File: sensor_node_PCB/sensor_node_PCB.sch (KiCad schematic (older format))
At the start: 23 parts

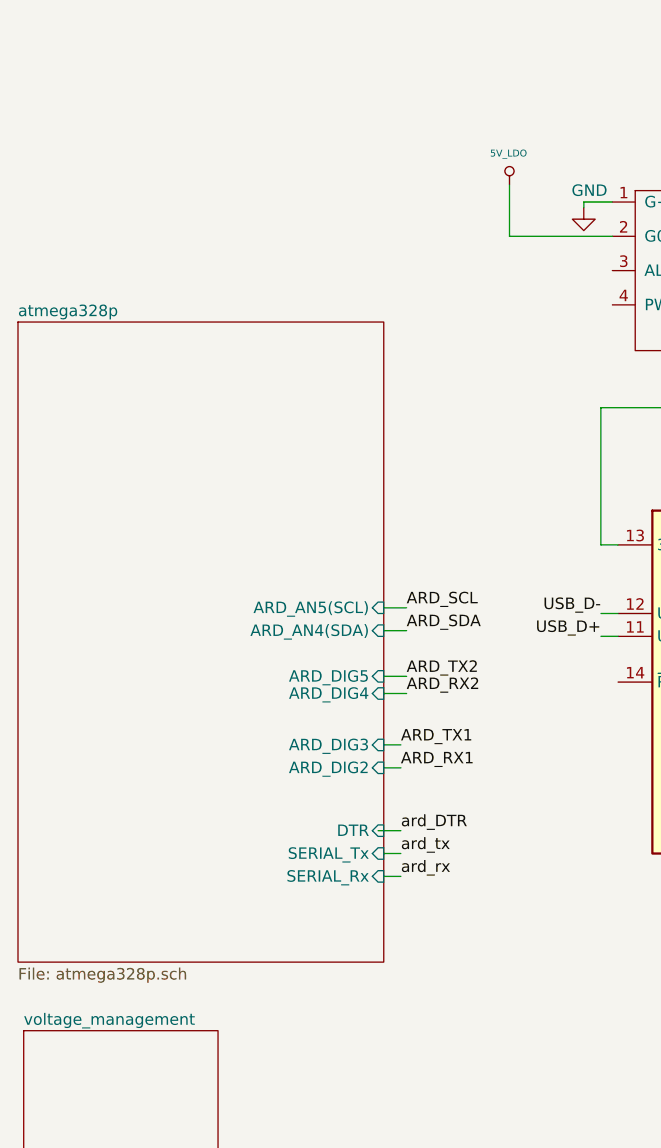
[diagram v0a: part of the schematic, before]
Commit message: ADDED BREAKOUT PINS
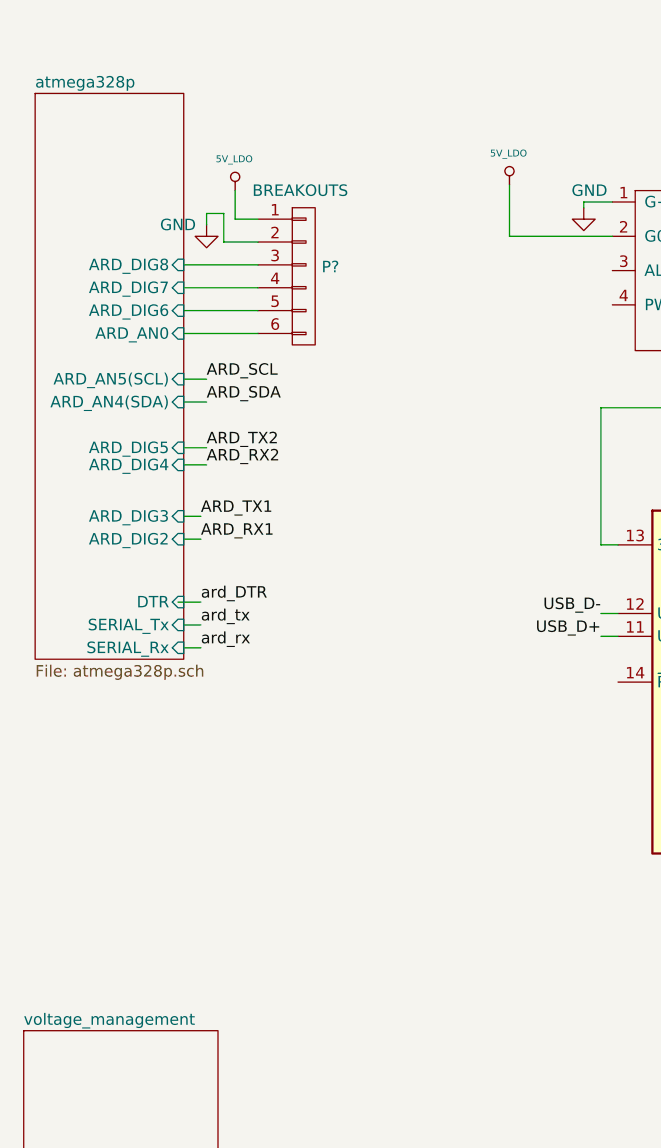
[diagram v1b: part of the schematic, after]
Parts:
- added P?: BREAKOUTS, symbol Arduino_Uno_R3_From_Scratch-rescue:CONN_01X06
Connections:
- net 5V_LDO: now also P?.1 (P1)
- net GND: now also P?.2 (P2)
- new net atmega328p/ARD_AN0: P?.6 (P6)
- new net atmega328p/ARD_DIG6: P?.5 (P5)
- new net atmega328p/ARD_DIG7: P?.4 (P4)
- new net atmega328p/ARD_DIG8: P?.3 (P3)
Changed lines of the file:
@@
 $EndComp
-$Sheet
-S 625  1825 1600 2800
-U 5F4E1E8A
-F0 "atmega328p" 50
-F1 "atmega328p.sch" 50
-F2 "SERIAL_Rx" I R 2225 4250 50
-F3 "SERIAL_Tx" I R 2225 4150 50
-F4 "DTR" I R 2225 4050 50
-F5 "ARD_DIG2" I R 2225 3775 50
-F6 "ARD_DIG3" I R 2225 3675 50
-F7 "ARD_DIG4" I R 2225 3450 50
-F8 "ARD_DIG5" I R 2225 3375 50
-F9 "ARD_AN4(SDA)" I R 2225 3175 50
-F10 "ARD_AN5(SCL)" I R 2225 3075 50
-$EndSheet
 $Sheet
 S 650  4925 850  850
@@
 	1    0    0    -1
 $EndComp
-Text Label 2300 4150 0    50   ~ 0
+Text Label 1425 3150 0    50   ~ 0
 ard_tx
 Wire Wire Line
-	2225 4150 2300 4150
-Text Label 2300 4250 0    50   ~ 0
+	1350 3150 1425 3150
+Text Label 1425 3250 0    50   ~ 0
 ard_rx
 Wire Wire Line
-	2225 4250 2300 4250
+	1350 3250 1425 3250
 Text Label 4750 2900 0    50   ~ 0
 ard_tx
@@
 Wire Wire Line
 	4650 2900 4750 2900
-Text Label 2300 4050 0    50   ~ 0
+Text Label 1425 3050 0    50   ~ 0
 ard_DTR
 Wire Wire Line
-	2200 4050 2300 4050
+	1325 3050 1425 3050
 Text Label 4750 3200 0    50   ~ 0
 ard_DTR
@@
 Wire Wire Line
 	4175 2500 4050 2500
-Text Label 2300 3675 0    50   ~ 0
+Text Label 1425 2675 0    50   ~ 0
 ARD_TX1
-Text Label 2300 3775 0    50   ~ 0
+Text Label 1425 2775 0    50   ~ 0
 ARD_RX1
 Wire Wire Line
-	2225 3775 2300 3775
-Wire Wire Line
-	2225 3675 2300 3675
+	1350 2775 1425 2775
+Wire Wire Line
+	1350 2675 1425 2675
 $Comp
 L Kicad_symbols:SP485EEN-L_TR U?
@@
 Wire Wire Line
 	3100 1300 3225 1300
-Text Label 2325 3375 0    50   ~ 0
+Text Label 1450 2375 0    50   ~ 0
 ARD_TX2
 Wire Wire Line
-	2225 3375 2325 3375
-Text Label 2325 3450 0    50   ~ 0
+	1350 2375 1450 2375
+Text Label 1450 2450 0    50   ~ 0
 ARD_RX2
 Wire Wire Line
-	2225 3450 2325 3450
+	1350 2450 1450 2450
 Text Label 4450 1600 0    50   ~ 0
 ARD_RX2
@@
 Wire Wire Line
 	9800 2950 9800 3000
-Text Label 2325 3075 0    50   ~ 0
+Text Label 1450 2075 0    50   ~ 0
 ARD_SCL
-Text Label 2325 3175 0    50   ~ 0
+Text Label 1450 2175 0    50   ~ 0
 ARD_SDA
 Wire Wire Line
-	2225 3075 2325 3075
-Wire Wire Line
-	2225 3175 2325 3175
+	1350 2075 1450 2075
+Wire Wire Line
+	1350 2175 1450 2175
 Text Label 10200 2600 0    50   ~ 0
 ARD_SCL
@@
 Wire Wire Line
 	10950 4300 10950 4375
+$Comp
+L Arduino_Uno_R3_From_Scratch-rescue:CONN_01X06 P?
+U 1 1 5F6DB19A
+P 1875 1625
+F 0 "P?" H 1953 1666 50  0000 L CNN
+F 1 "BREAKOUTS" H 1650 2000 50  0000 L CNN
+F 2 "" H 1875 1625 60  0000 C CNN
+F 3 "" H 1875 1625 60  0000 C CNN
+	1    1875 1625
+	1    0    0    -1
+$EndComp
+$Comp
+L Arduino_Uno_R3_From_Scratch-rescue:5V_LDO #PWR?
+U 1 1 5F6DDE3C
+P 1575 1250
+F 0 "#PWR?" H 1575 1340 20  0001 C CNN
+F 1 "5V_LDO" H 1571 1388 30  0000 C CNN
+F 2 "" H 1575 1250 60  0000 C CNN
+F 3 "" H 1575 1250 60  0000 C CNN
+	1    1575 1250
+	1    0    0    -1
+$EndComp
+$Comp
+L Arduino_Uno_R3_From_Scratch-rescue:GND #PWR?
+U 1 1 5F6DF1FF
+P 1450 1400
+F 0 "#PWR?" H 1450 1150 50  0001 C CNN
+F 1 "GND" H 1325 1400 50  0000 C CNN
+F 2 "" H 1450 1400 60  0000 C CNN
+F 3 "" H 1450 1400 60  0000 C CNN
+	1    1450 1400
+	1    0    0    -1
+$EndComp
+Wire Wire Line
+	1575 1250 1575 1375
+Wire Wire Line
+	1575 1375 1675 1375
+Wire Wire Line
+	1675 1475 1525 1475
+Wire Wire Line
+	1525 1475 1525 1350
+Wire Wire Line
+	1525 1350 1450 1350
+Wire Wire Line
+	1450 1350 1450 1400
+Wire Wire Line
+	1350 1575 1675 1575
+Wire Wire Line
+	1350 1675 1675 1675
+Wire Wire Line
+	1350 1775 1675 1775
+Wire Wire Line
+	1350 1875 1675 1875
+$Sheet
+S 700  825  650  2475
+U 5F4E1E8A
+F0 "atmega328p" 50
+F1 "atmega328p.sch" 50
+F2 "SERIAL_Rx" I R 1350 3250 50
+F3 "SERIAL_Tx" I R 1350 3150 50
+F4 "DTR" I R 1350 3050 50
+F5 "ARD_DIG2" I R 1350 2775 50
+F6 "ARD_DIG3" I R 1350 2675 50
+F7 "ARD_DIG4" I R 1350 2450 50
+F8 "ARD_DIG5" I R 1350 2375 50
+F9 "ARD_AN4(SDA)" I R 1350 2175 50
+F10 "ARD_AN5(SCL)" I R 1350 2075 50
+F11 "ARD_DIG6" I R 1350 1775 50
+F12 "ARD_DIG7" I R 1350 1675 50
+F13 "ARD_DIG8" I R 1350 1575 50
+F14 "ARD_AN0" I R 1350 1875 50
+$EndSheet
 $EndSCHEMATC

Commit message: schematic finished
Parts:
- added C?: 1uF, ~, symbol Arduino_Uno_R3_From_Scratch-rescue:C
- added C?: 0.1 uF, ~, symbol Arduino_Uno_R3_From_Scratch-rescue:C
- added C?: 4.7uF, ~, symbol Arduino_Uno_R3_From_Scratch-rescue:C
- added Q?: FDN340P, ~, symbol Arduino_Uno_R3_From_Scratch-rescue:Q_PMOS_GSD
- added R? (x2): 10K, ~, symbol Arduino_Uno_R3_From_Scratch-rescue:R
- added U?: LMV358IDGKR, ~, symbol Arduino_Uno_R3_From_Scratch-rescue:LM358
- added U?: LM1117-3.3, symbol Regulator_Linear:LM1117-3.3
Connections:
- net 3V3_LDO: now also C?.1, U?.2 (-), U?.2 (VO)
- net 5V_LDO: now also C?.1, C?.2, Q?.2 (S), U?.3 (VI), U?.8 (V+)
- net GND: now also C?.1, C?.2, C?.2, R?.1, U?.1 (GND), U?.4 (V-)
- net USBVCC: now also Q?.3 (D)
- net Vin: now also R?.2
- net at U?.13 (3V3OUT), U?.3 (VCCIO): now also U?.14 (~RESET)
- new net: R?.1, R?.2, U?.3 (+)
- new net: Q?.1 (G), U?.1
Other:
- moved on the sheet: C?, D?, F?, J?, Q?, R?, U?

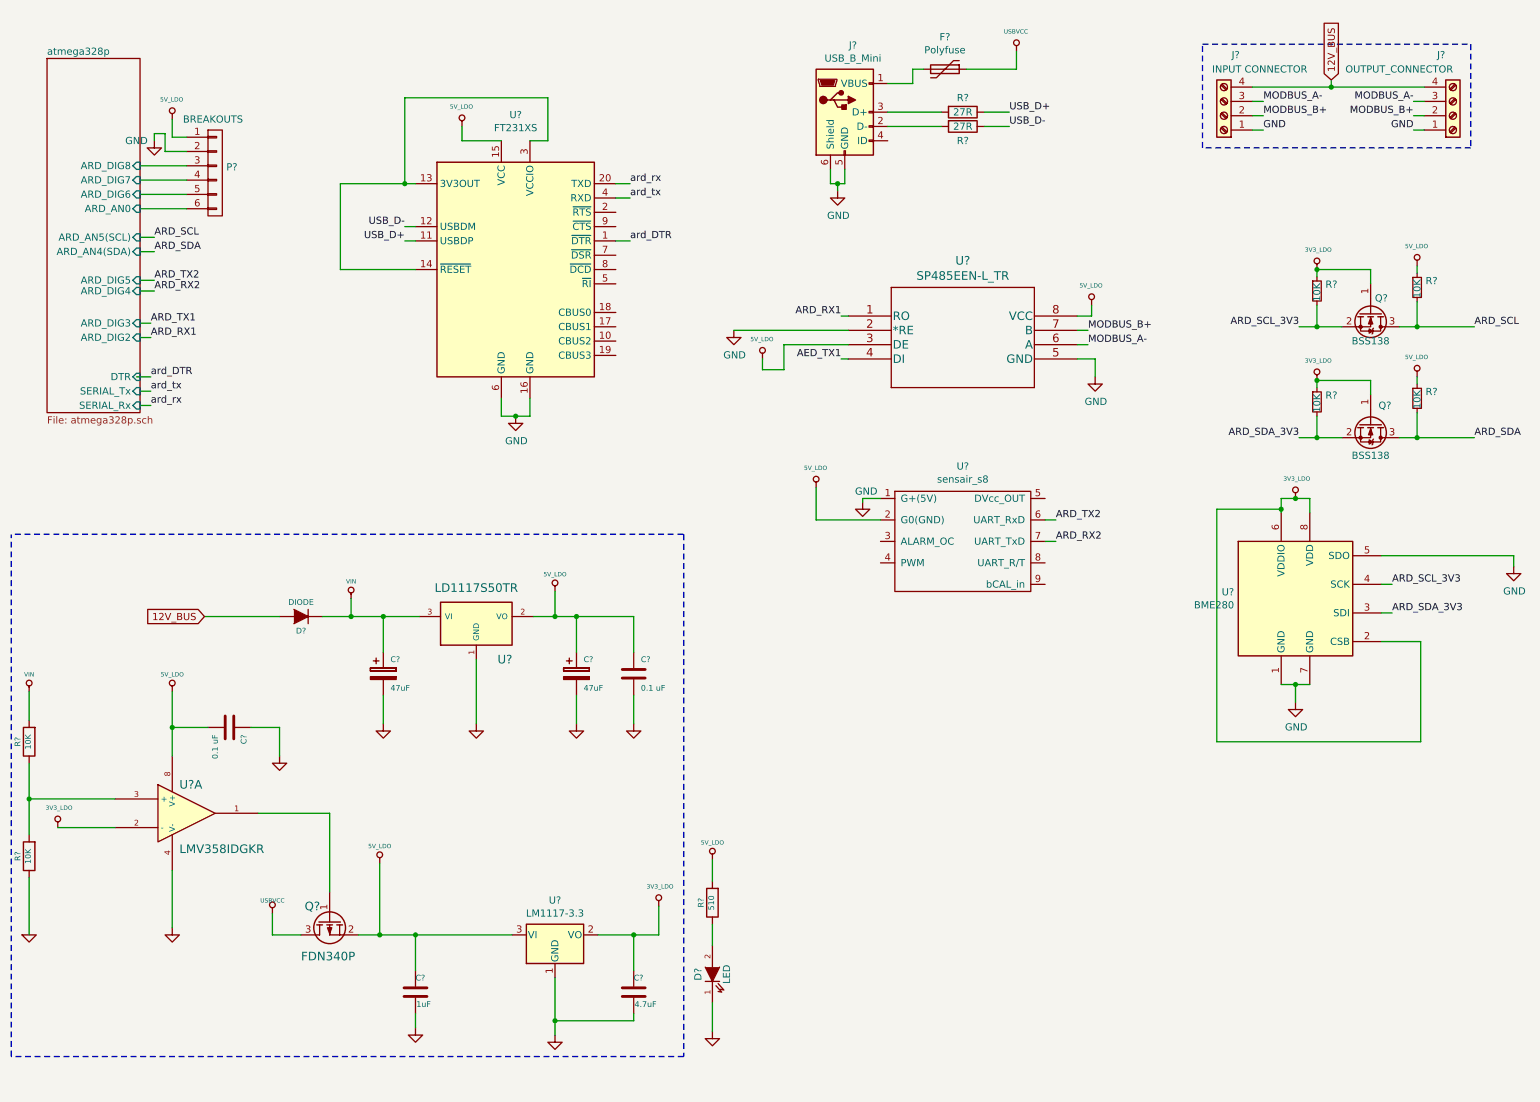
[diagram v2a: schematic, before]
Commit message: assign footprints 80% completed
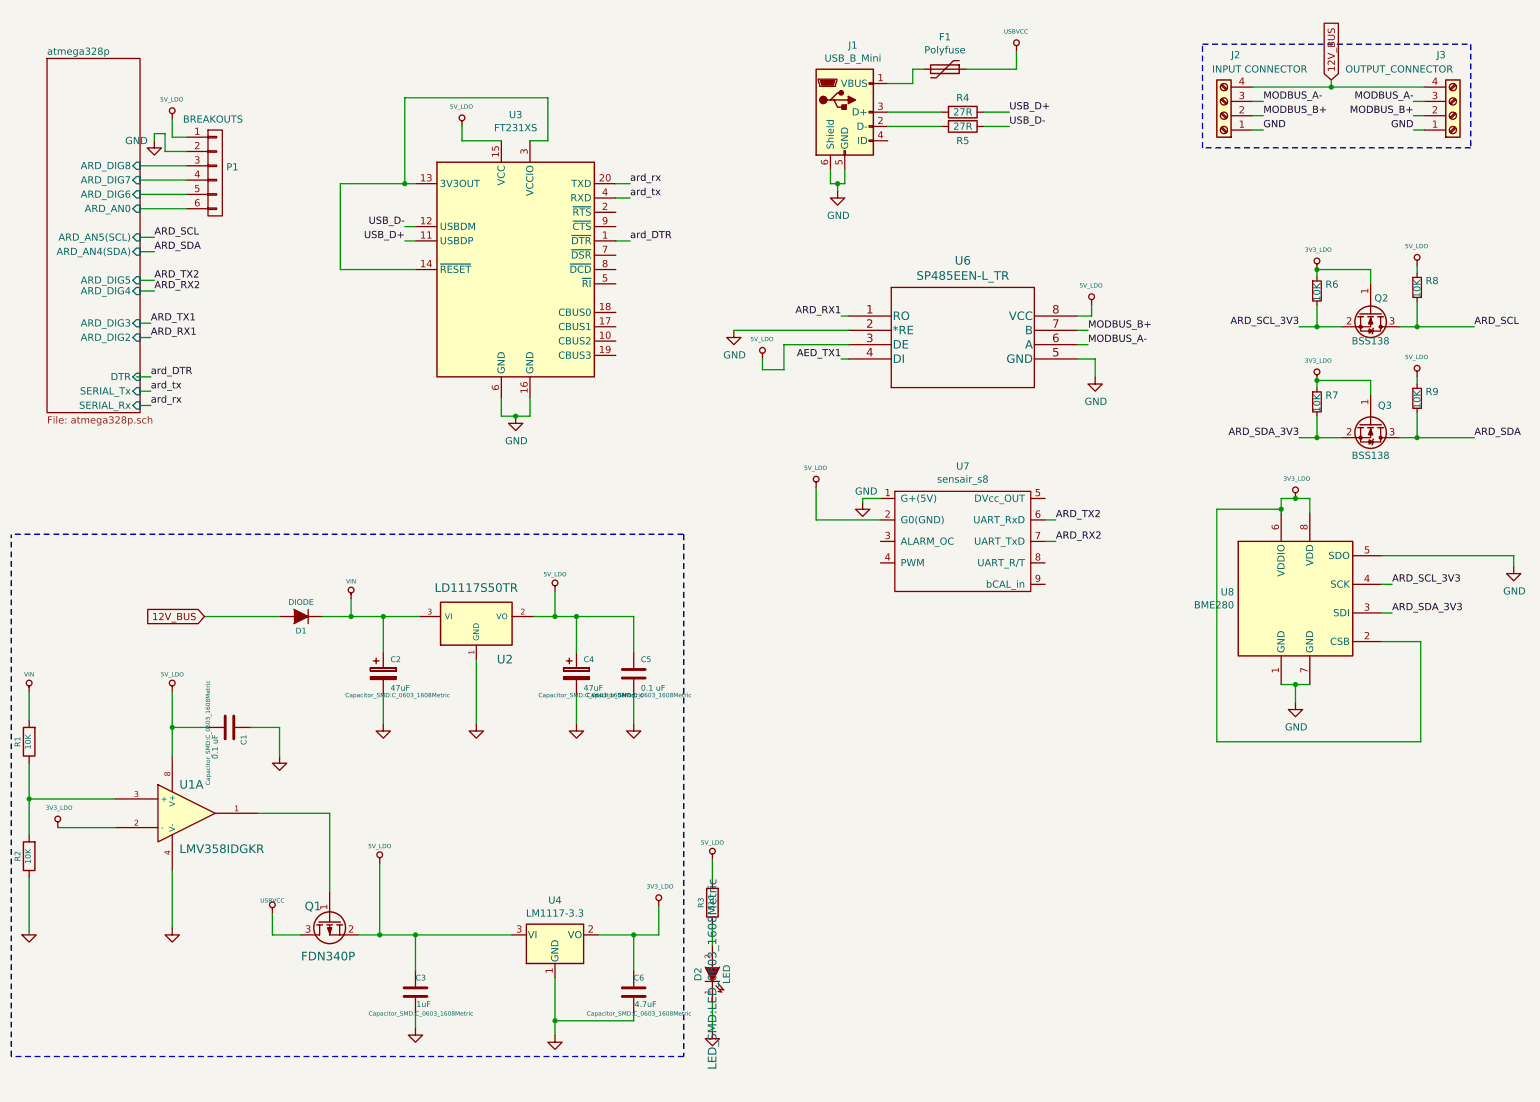
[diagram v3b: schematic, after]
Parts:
- C1, C2, C3, C4, C5, C6: renamed from C?; footprint ~ -> Capacitor_SMD:C_0603_1608Metric
- D1: renamed from D?; footprint ~ -> (none)
- D2: renamed from D?; footprint ~ -> LED_SMD:LED_0603_1608Metric
- F1: renamed from F?; footprint (none) -> Fuse:Fuse_1206_3216Metric
- J1: renamed from J?; footprint (none) -> Connector_USB:USB_Mini-B_Wuerth_65100516121_Horizontal
- P1: renamed from P?; footprint (none) -> Connector_PinHeader_2.54mm:PinHeader_1x06_P2.54mm_Vertical
- Q1: renamed from Q?; footprint ~ -> Package_TO_SOT_SMD:SuperSOT-3
- R1, R2, R3: renamed from R?; footprint ~ -> Resistor_SMD:R_0603_1608Metric
- R4, R5, R6, R7, R8, R9: renamed from R?; footprint (none) -> Resistor_SMD:R_0603_1608Metric
- U1: renamed from U?; footprint ~ -> Package_SO:SOIC-8_3.9x4.9mm_P1.27mm
- U2, U4: renamed from U?; footprint (none) -> Package_TO_SOT_SMD:SOT-223-3_TabPin2
- U6: renamed from U?; footprint NSOIC-8 -> Package_SO:SOIC-8_3.9x4.9mm_P1.27mm
- gave numbers to parts that had none: 7

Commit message: routing started 15%
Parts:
- D1: footprint (none) -> Diode_SMD:D_SOD-123
- J2, J3: footprint (none) -> Connector_Phoenix_MSTB:PhoenixContact_MSTB_2,5_4-GF-5,08_1x04_P5.08mm_Horizontal_ThreadedFlange
- P1: footprint Connector_PinHeader_2.54mm:PinHeader_1x06_P2.54mm_Vertical -> TerminalBlock_Phoenix:TerminalBlock_Phoenix_MPT-0,5-6-2.54_1x06_P2.54mm_Horizontal
- U7: footprint (none) -> kicad_footprints:senseair_s8_v3
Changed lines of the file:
@@
 F 0 "J2" H 8843 800 50  0000 C CNN
 F 1 "INPUT CONNECTOR" H 8675 900 50  0000 C CNN
-F 2 "" H 8925 1225 50  0001 C CNN
+F 2 "Connector_Phoenix_MSTB:PhoenixContact_MSTB_2,5_4-GF-5,08_1x04_P5.08mm_Horizontal_ThreadedFlange" H 8925 1225 50  0001 C CNN
 F 3 "~" H 8925 1225 50  0001 C CNN
 	1    8925 1225
@@
 F 0 "J3" H 10443 800 50  0000 C CNN
 F 1 "OUTPUT_CONNECTOR" H 10150 900 50  0000 C CNN
-F 2 "" H 10525 1225 50  0001 C CNN
+F 2 "Connector_Phoenix_MSTB:PhoenixContact_MSTB_2,5_4-GF-5,08_1x04_P5.08mm_Horizontal_ThreadedFlange" H 10525 1225 50  0001 C CNN
 F 3 "~" H 10525 1225 50  0001 C CNN
 	1    10525 1225
@@
 F 0 "D1" H 2475 4825 40  0000 C CNN
 F 1 "DIODE" H 2475 4625 40  0000 C CNN
-F 2 "" H 2475 4725 60  0001 C CNN
+F 2 "Diode_SMD:D_SOD-123" H 2475 4725 60  0001 C CNN
 F 3 "http://www.onsemi.com/pub_link/Collateral/MRA4003T3-D.PDF" H 2475 4725 60  0001 C CNN
 F 4 "1A, 1000V, SILICON, SIGNAL DIODE, ROHS COMPLIANT, COMPACT, PLASTIC, CASE 403D-02, SMA, 2 PIN" H 2475 4725 60  0001 C CNN "Characteristics"
@@
 F 0 "U7" H 7100 4525 50  0000 C CNN
 F 1 "sensair_s8" H 7100 4434 50  0000 C CNN
-F 2 "" H 6925 4100 50  0001 C CNN
+F 2 "kicad_footprints:senseair_s8_v3" H 6925 4100 50  0001 C CNN
 F 3 "" H 6925 4100 50  0001 C CNN
 	1    7075 4100
@@
 F 0 "P1" H 1953 1666 50  0000 L CNN
 F 1 "BREAKOUTS" H 1650 2000 50  0000 L CNN
-F 2 "Connector_PinHeader_2.54mm:PinHeader_1x06_P2.54mm_Vertical" H 1875 1625 60  0001 C CNN
+F 2 "TerminalBlock_Phoenix:TerminalBlock_Phoenix_MPT-0,5-6-2.54_1x06_P2.54mm_Horizontal" H 1875 1625 60  0001 C CNN
 F 3 "" H 1875 1625 60  0000 C CNN
 	1    1875 1625

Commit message: routing 50%
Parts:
- J1: footprint Connector_USB:USB_Mini-B_Wuerth_65100516121_Horizontal -> Connector_USB:USB_Mini-B_Tensility_54-00023_Vertical
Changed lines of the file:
@@
 F 0 "J1" H 6332 1667 50  0000 C CNN
 F 1 "USB_B_Mini" H 6332 1576 50  0000 C CNN
-F 2 "Connector_USB:USB_Mini-B_Wuerth_65100516121_Horizontal" H 6425 1150 50  0001 C CNN
+F 2 "Connector_USB:USB_Mini-B_Tensility_54-00023_Vertical" H 6425 1150 50  0001 C CNN
 F 3 "~" H 6425 1150 50  0001 C CNN
 	1    6275 1200

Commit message: routing 60% completed
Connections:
- net AED_TX1 is gone; now on net ARD_TX1: U6.4 (DI)
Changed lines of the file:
@@
 $EndComp
 Text Label 6250 2925 2    50   ~ 0
-AED_TX1
+ARD_TX1
 Text Label 6250 2625 2    50   ~ 0
 ARD_RX1

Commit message: fixed senseair s8 pin mixup - added lots of silk text
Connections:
- net 5V_LDO: now also U7.1 (G+(5V)); no longer U7.2 (G0(GND))
- net GND: now also U7.2 (G0(GND)); no longer U7.1 (G+(5V))
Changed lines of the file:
@@
 Wire Wire Line
 	4675 1800 4775 1800
-Text Label 1425 3050 0    50   ~ 0
+Text Label 1450 3050 0    50   ~ 0
 ard_DTR
-Wire Wire Line
-	1325 3050 1425 3050
 Text Label 4775 2100 0    50   ~ 0
 ard_DTR
@@
 	1    0    0    -1
 $EndComp
-Wire Wire Line
-	6075 3825 6075 4050
-Wire Wire Line
-	6075 4050 6525 4050
-$Comp
-L Arduino_Uno_R3_From_Scratch-rescue:GND #PWR0120
-U 1 1 5F5191A0
-P 6400 3925
-F 0 "#PWR0120" H 6400 3675 50  0001 C CNN
-F 1 "GND" H 6425 4000 50  0000 C CNN
-F 2 "" H 6400 3925 60  0000 C CNN
-F 3 "" H 6400 3925 60  0000 C CNN
-	1    6400 3925
-	1    0    0    -1
-$EndComp
-Wire Wire Line
-	6400 3925 6400 3900
-Wire Wire Line
-	6400 3900 6525 3900
 Text Label 1450 2375 0    50   ~ 0
 ARD_TX2
@@
 F2 "SERIAL_Rx" I R 1350 3250 50
 F3 "SERIAL_Tx" I R 1350 3150 50
-F4 "DTR" I R 1350 3050 50
-F5 "ARD_DIG2" I R 1350 2775 50
-F6 "ARD_DIG3" I R 1350 2675 50
-F7 "ARD_DIG4" I R 1350 2450 50
-F8 "ARD_DIG5" I R 1350 2375 50
-F9 "ARD_AN4(SDA)" I R 1350 2175 50
-F10 "ARD_AN5(SCL)" I R 1350 2075 50
-F11 "ARD_DIG6" I R 1350 1775 50
-F12 "ARD_DIG7" I R 1350 1675 50
-F13 "ARD_DIG8" I R 1350 1575 50
-F14 "ARD_AN0" I R 1350 1875 50
+F4 "ARD_DIG2" I R 1350 2775 50
+F5 "ARD_DIG3" I R 1350 2675 50
+F6 "ARD_DIG4" I R 1350 2450 50
+F7 "ARD_DIG5" I R 1350 2375 50
+F8 "ARD_AN4(SDA)" I R 1350 2175 50
+F9 "ARD_AN5(SCL)" I R 1350 2075 50
+F10 "ARD_DIG6" I R 1350 1775 50
+F11 "ARD_DIG7" I R 1350 1675 50
+F12 "ARD_DIG8" I R 1350 1575 50
+F13 "ARD_AN0" I R 1350 1875 50
+F14 "DTR" I R 1350 3050 50
 $EndSheet
 Wire Wire Line
@@
 Wire Notes Line
 	450  7800 450  4150
+Wire Wire Line
+	1350 3050 1450 3050
+Wire Wire Line
+	6075 3825 6075 3900
+Wire Wire Line
+	6075 3900 6525 3900
+$Comp
+L Arduino_Uno_R3_From_Scratch-rescue:GND #PWR?
+U 1 1 5F5AAEA2
+P 6275 4050
+F 0 "#PWR?" H 6275 3800 50  0001 C CNN
+F 1 "GND" H 6280 3877 50  0000 C CNN
+F 2 "" H 6275 4050 60  0000 C CNN
+F 3 "" H 6275 4050 60  0000 C CNN
+	1    6275 4050
+	1    0    0    -1
+$EndComp
+Wire Wire Line
+	6275 4050 6525 4050
 $EndSCHEMATC
